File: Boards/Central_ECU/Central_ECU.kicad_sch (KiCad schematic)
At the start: 85 parts, among them J1 Micro_SD_Card, U1 SSD1306, U2 STM32G0B1RCTx, U3 TCAN1046, Y1 8MHz, Y2 32.768k

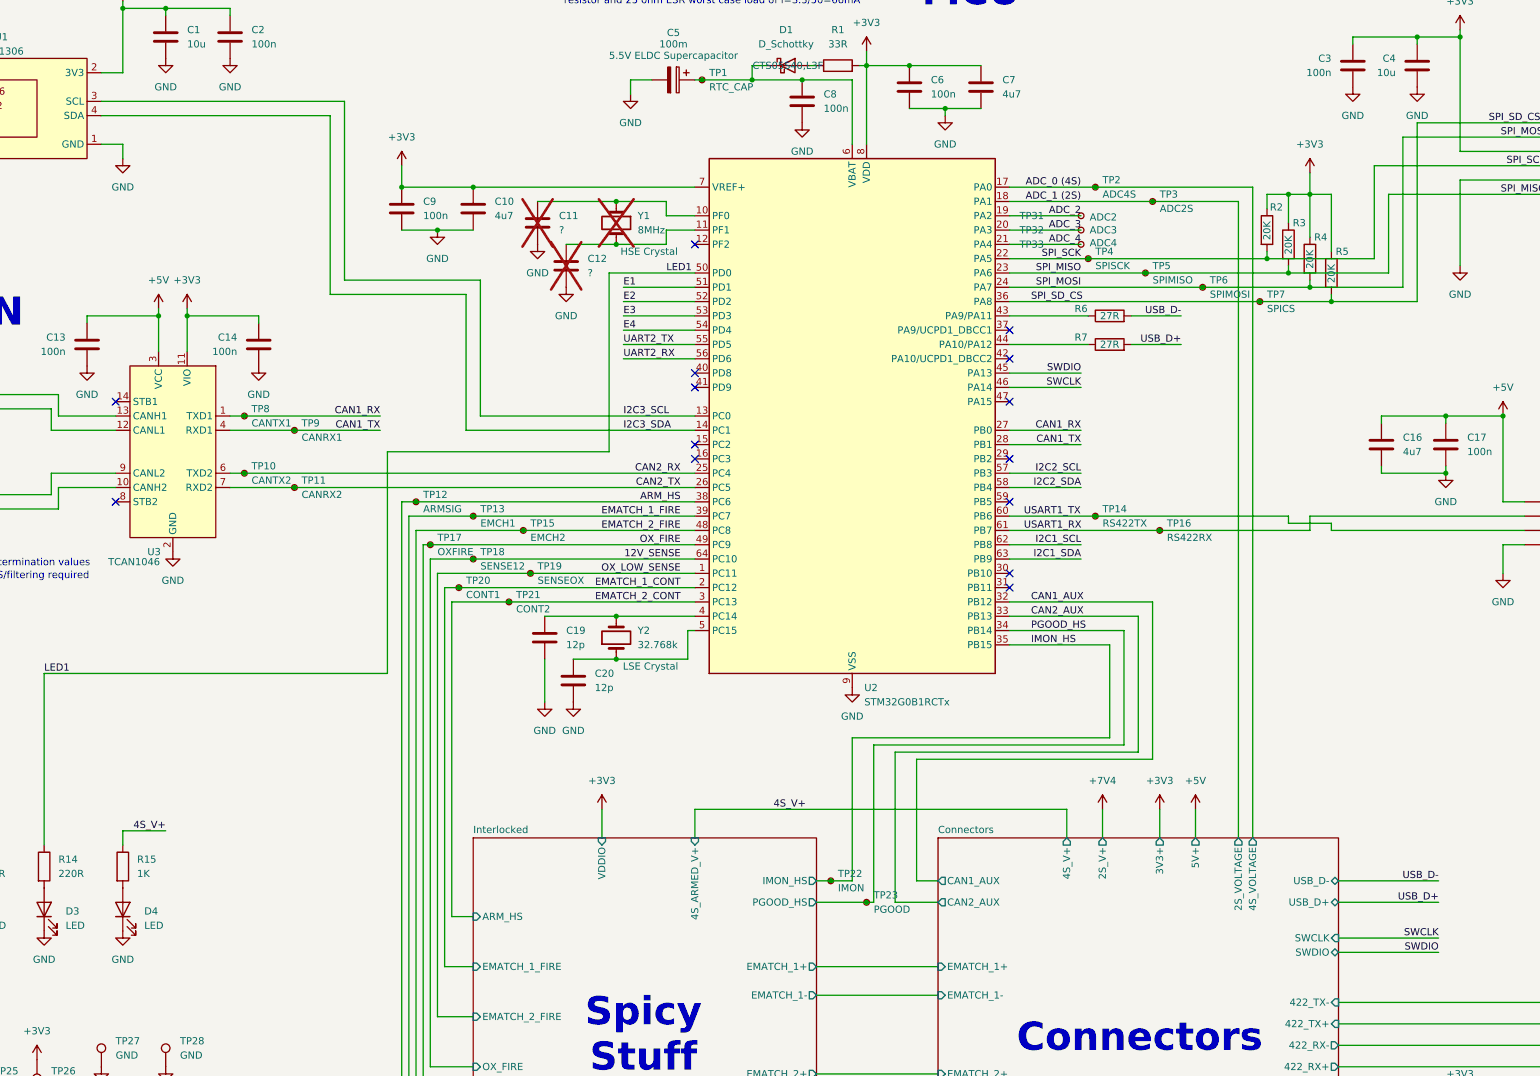
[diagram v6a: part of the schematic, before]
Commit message: Changed to 0603 passives and added NRST line
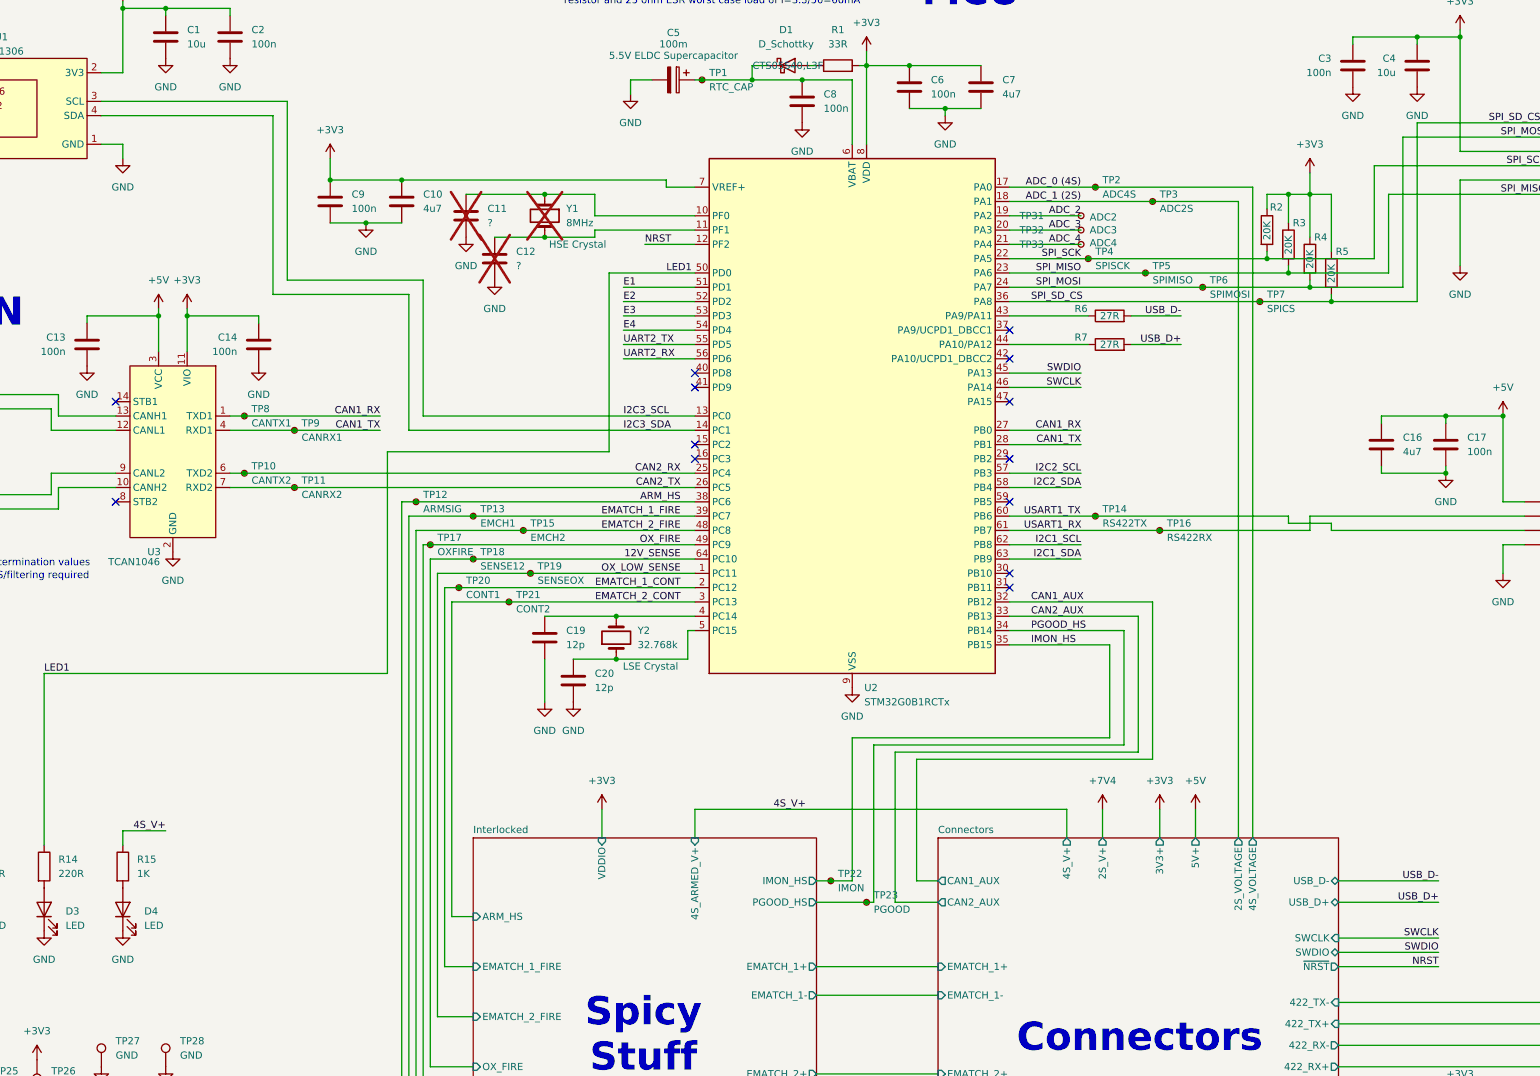
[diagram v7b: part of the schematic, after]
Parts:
- C1, C10, C13, C14, C15, C16, C17, C18, C2, C3, C4, C6, C7, C8, C9: footprint Capacitor_SMD:C_0805_2012Metric -> Capacitor_SMD:C_0603_1608Metric
- R1, R10, R11, R12, R13, R14, R15, R16, R17, R18, R19, R2, R3, R4, R5, R6, R7, R8, R9: footprint Resistor_SMD:R_0805_2012Metric -> Resistor_SMD:R_0603_1608Metric
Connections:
- net NRST: now reaches U2.12 (PF2)
- no-connect marks 16 -> 15
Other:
- sheet Connectors ports: added ~{NRST}; removed none
- moved on the sheet: C10, C11, C12, C9, Y1

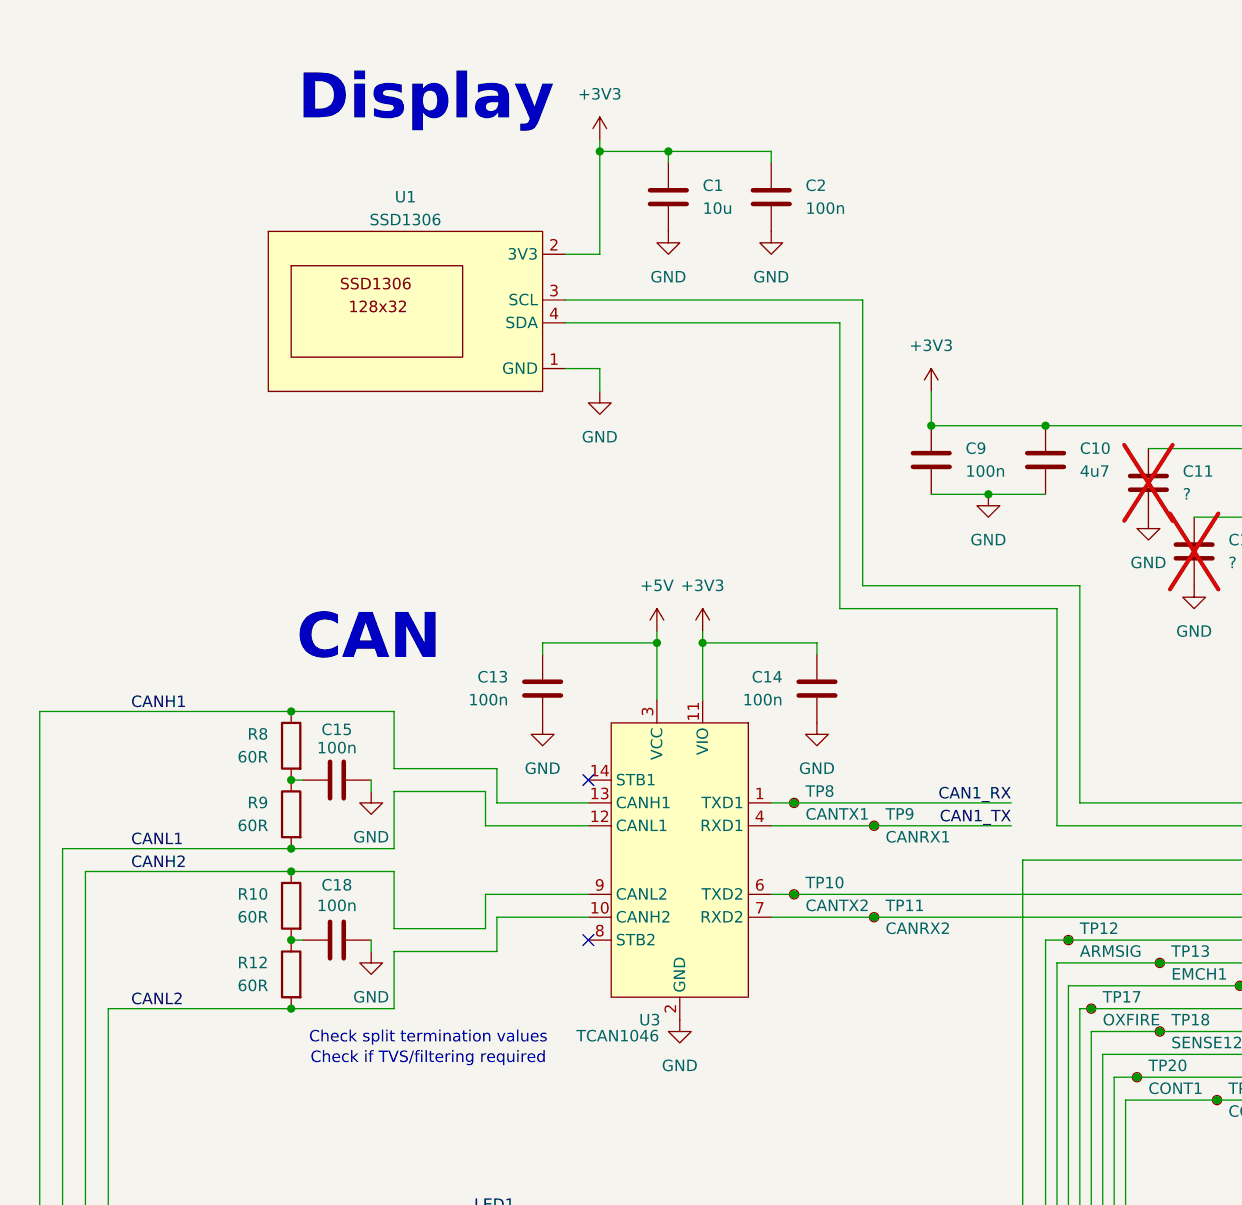
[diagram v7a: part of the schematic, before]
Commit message: Added environmental P+T sensor
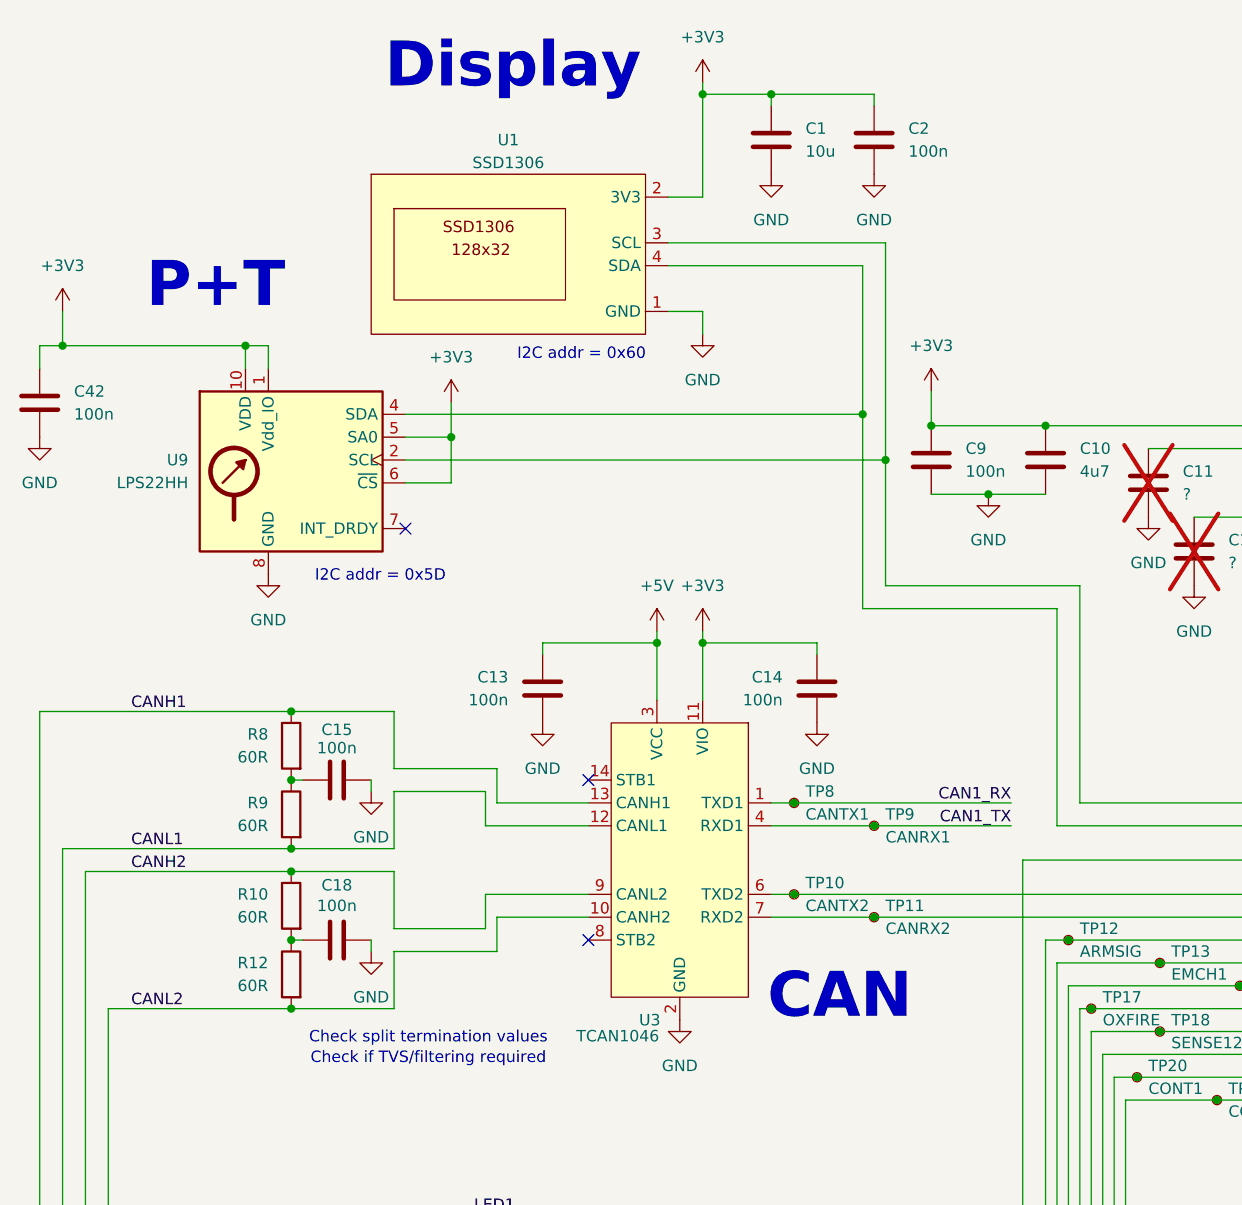
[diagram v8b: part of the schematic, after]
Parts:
- added C42: 100n, Capacitor_SMD:C_0603_1608Metric, symbol Device:C
- added U9: LPS22HH, Package_LGA:ST_HLGA-10_2x2mm_P0.5mm_LayoutBorder3x2y, symbol Sensor_Pressure:LPS22HH
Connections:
- net +3V3: now also C42.1, U9.1 (Vdd_IO), U9.10 (VDD), U9.5 (SA0), U9.6 (~{CS})
- net GND: now also C42.2, U9.3 (GND), U9.8 (GND), U9.9 (GND)
- net I2C3_SCL: now also U9.2 (SCL)
- net I2C3_SDA: now also U9.4 (SDA)
- no-connect marks 15 -> 16
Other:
- note added: "I2C addr = 0x5D"
- note added: "I2C addr = 0x60"
- note added: "P+T"
- moved on the sheet: C1, C2, U1
